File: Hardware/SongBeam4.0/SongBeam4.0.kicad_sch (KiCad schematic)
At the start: 140 parts, among them J1 Conn_01x02, J10 732511150, J11 Conn_01x02, J12 Conn_01x02, J13 Conn_01x01, J2 RJ45, J3 RJ45, J4 Conn_01x07, J5 Conn_01x04, J6 Conn_01x07, J7 Conn_01x04, J8 Conn_01x06, J9 USB_B_Micro, Q2 DTC143ZEBTL, SW2 PTS815 SJM 250 SMTR LFS, SW3 PTS815 SJM 250 SMTR LFS, U1 IM66D132H, U10 Teensy4.1, U11 BQ25185DLHR, U12 AO6604, U13 TPS62842DGRR, U14 TPL5111DDCR, U15 AO6604, U16 TXS0108EPW, U17 LP5907MFX-1.8/NOPB, U19 L86-M33, U2 IM66D132H, U20 AO3407A, U3 IM66D132H, U4 IM66D132H, U5 IM66D132H, U6 IM66D132H, U7 IM66D132H, U8 IM66D132H, U9 PCMD3180IRTWR

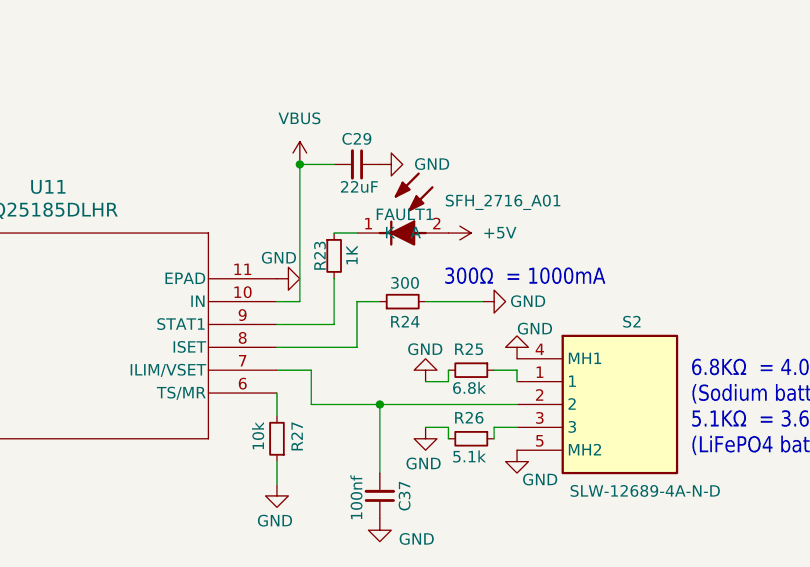
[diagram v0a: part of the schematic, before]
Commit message: bom main board update
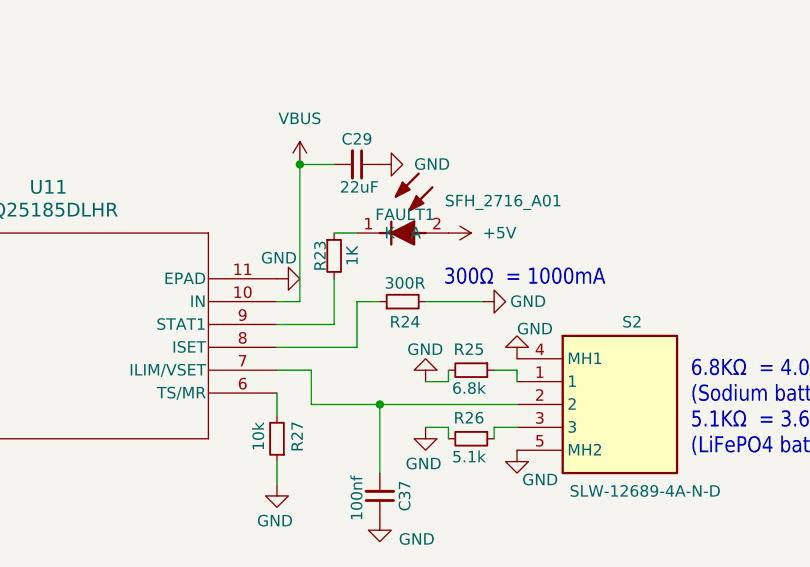
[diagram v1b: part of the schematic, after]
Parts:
- R24: value 300 -> 300R
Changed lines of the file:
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@@
 		(company "Royal Holloway")
 		(comment 1 "Creative Commons Attribution 4.0 International License")
-		(comment 2 "Sohil, Saaria., Lachlan, Robert.")
+		(comment 2 "Lachlan, Robert.")
 		(comment 3 "Q. Oliva, Marcos., Lies, Zandberg.,")
 	)
@@
 			)
 		)
-		(property "Value" "300"
+		(property "Value" "300R"
 			(at 132.334 191.008 90)
 			(effects

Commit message: added a version for manual routing
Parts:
- added F1: Polyfuse, MINISMDC050F-2:MINISMDC050F2, symbol Device:Polyfuse
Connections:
- net PWR is gone; now on net +3.3V: J1.1 (Pin_1), JP1.2 (B), U10.48 (VIN)
- net +5V: now also C41.1, R28.1, TP1.1, U12.2 (S2), U13.5 (EN), U13.6 (VIN); no longer F3.1
- net VBAT: now also F1.2; no longer C27.2, U11.2 (BAT)
- net VBUS: now also F3.2; no longer C29.2, U11.10 (IN)
- new net: C29.2, F3.1, U11.10 (IN)
- new net: C27.2, F1.1, U11.2 (BAT)
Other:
- moved on the sheet: C27, C29, F3
